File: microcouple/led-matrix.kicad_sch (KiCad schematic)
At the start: 69 parts, among them U5 IS31FL3729

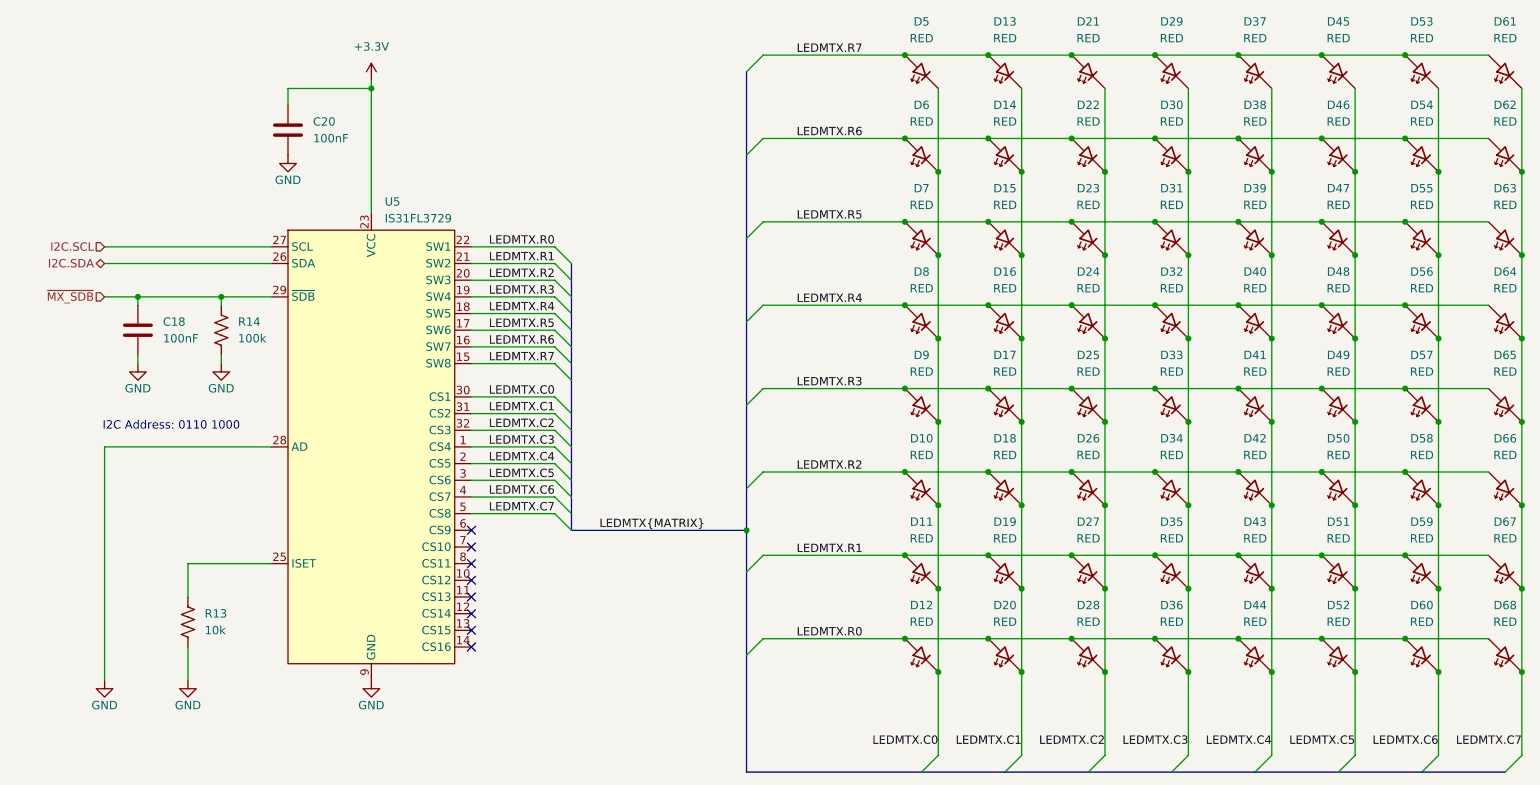
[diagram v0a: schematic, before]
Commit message: Update for JLCPCB
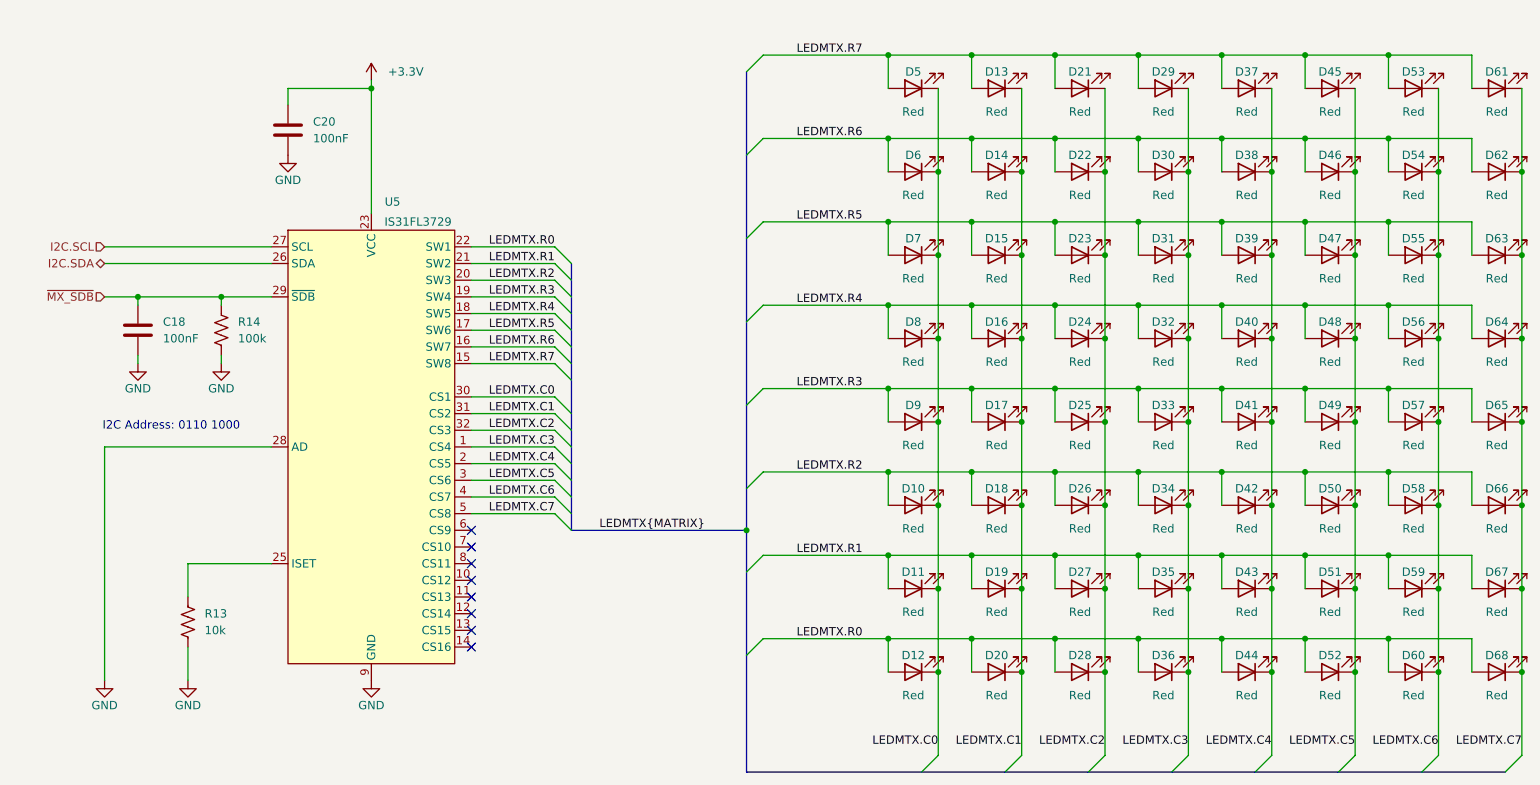
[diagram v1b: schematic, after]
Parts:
- C18, C20: footprint GS_SMD:0201_0603Metric -> GS_Capacitors:C_0201_0603Metric; symbol Device:C -> GS_Capacitor_0201:C_0201_100nF; LCSC ID (none) -> C18164587; Manufacturer (none) -> CCTC; Mfr. Part # (none) -> TCC0201X5R104M250ZT; Package (none) -> 0201
- D10, D11, D12, D13, D14, D15, D16, D17, D18, D19, D20, D21, D22, D23, D24, D25, D26, D27, D28, D29, D30, D31, D32, D33, D34, D35, D36, D37, D38, D39, D40, D41, D42, D43, D44, D45, D46, D47, D48, D49, D5, D50, D51, D52, D53, D54, D55, D56, D57, D58, D59, D6, D60, D61, D62, D63, D64, D65, D66, D67, D68, D7, D8, D9: value RED -> Red; symbol Device:LED_45deg -> GS_Optoelectronic:LED_0201_Red; LCSC ID (none) -> C3646923; Manufacturer (none) -> XINGLIGHT; Mfr. Part # (none) -> XL-0201SURC; Package (none) -> 0201
- R13: footprint GS_SMD:0201_0603Metric -> GS_Resistors:R_0201_0603Metric; symbol Device:R_US -> GS_Resistor_0201:R_0201_10k; LCSC ID (none) -> C304504; Manufacturer (none) -> FH (Guangdong Fenghua Advanced Tech); Mfr. Part # (none) -> RC-01W103JT; Package (none) -> 0201
- R14: footprint GS_SMD:0201_0603Metric -> GS_Resistors:R_0201_0603Metric; symbol Device:R_US -> GS_Resistor_0201:R_0201_100k; LCSC ID (none) -> C106224; Manufacturer (none) -> YAGEO; Mfr. Part # (none) -> RC0201FR-07100KL; Package (none) -> 0201
- U5: Manufacturer (none) -> ISSI(Integrated Silicon Solution); Mfr. Part # (none) -> IS31FL3729-QFLS4-TR; Package (none) -> QFN-32-EP(4x4)
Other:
- title: (none) -> LED Matrix

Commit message: Change all components to 0402 if smaller
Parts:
- C18, C20: footprint GS_Capacitors:C_0201_0603Metric -> GS_Capacitors:C_0402_1005Metric; symbol GS_Capacitor_0201:C_0201_100nF -> GS_Capacitor_0402:C_0402_100nF; LCSC ID C18164587 -> C344189; Mfr. Part # TCC0201X5R104M250ZT -> TCC0402X5R104K160AT; Package 0201 -> 0402
- D10, D11, D12, D13, D14, D15, D16, D17, D18, D19, D20, D21, D22, D23, D24, D25, D26, D27, D28, D29, D30, D31, D32, D33, D34, D35, D36, D37, D38, D39, D40, D41, D42, D43, D44, D45, D46, D47, D48, D49, D5, D50, D51, D52, D53, D54, D55, D56, D57, D58, D59, D6, D60, D61, D62, D63, D64, D65, D66, D67, D68, D7, D8, D9: footprint GS_Optoelectronics:LED_0201_0603Metric -> GS_Optoelectronics:LED_0402_1005Metric; symbol GS_Optoelectronic:LED_0201_Red -> GS_Optoelectronic:LED_0402_Red; LCSC ID C3646923 -> C965790; Mfr. Part # XL-0201SURC -> XL-1005SURC; Package 0201 -> 0402
- R13: footprint GS_Resistors:R_0201_0603Metric -> GS_Resistors:R_0402_1005Metric; symbol GS_Resistor_0201:R_0201_10k -> GS_Resistor_0402:R_0402_10k; LCSC ID C304504 -> C102759; Manufacturer FH (Guangdong Fenghua Advanced Tech) -> RALEC; Mfr. Part # RC-01W103JT -> RTT02103JTH; Package 0201 -> 0402
- R14: footprint GS_Resistors:R_0201_0603Metric -> GS_Resistors:R_0402_1005Metric; symbol GS_Resistor_0201:R_0201_100k -> GS_Resistor_0402:R_0402_100k; LCSC ID C106224 -> C3017514; Manufacturer YAGEO -> VO; Mfr. Part # RC0201FR-07100KL -> SCR0402J100K; Package 0201 -> 0402
